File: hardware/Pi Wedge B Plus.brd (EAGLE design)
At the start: 74.9 x 67.3 mm, 14 parts

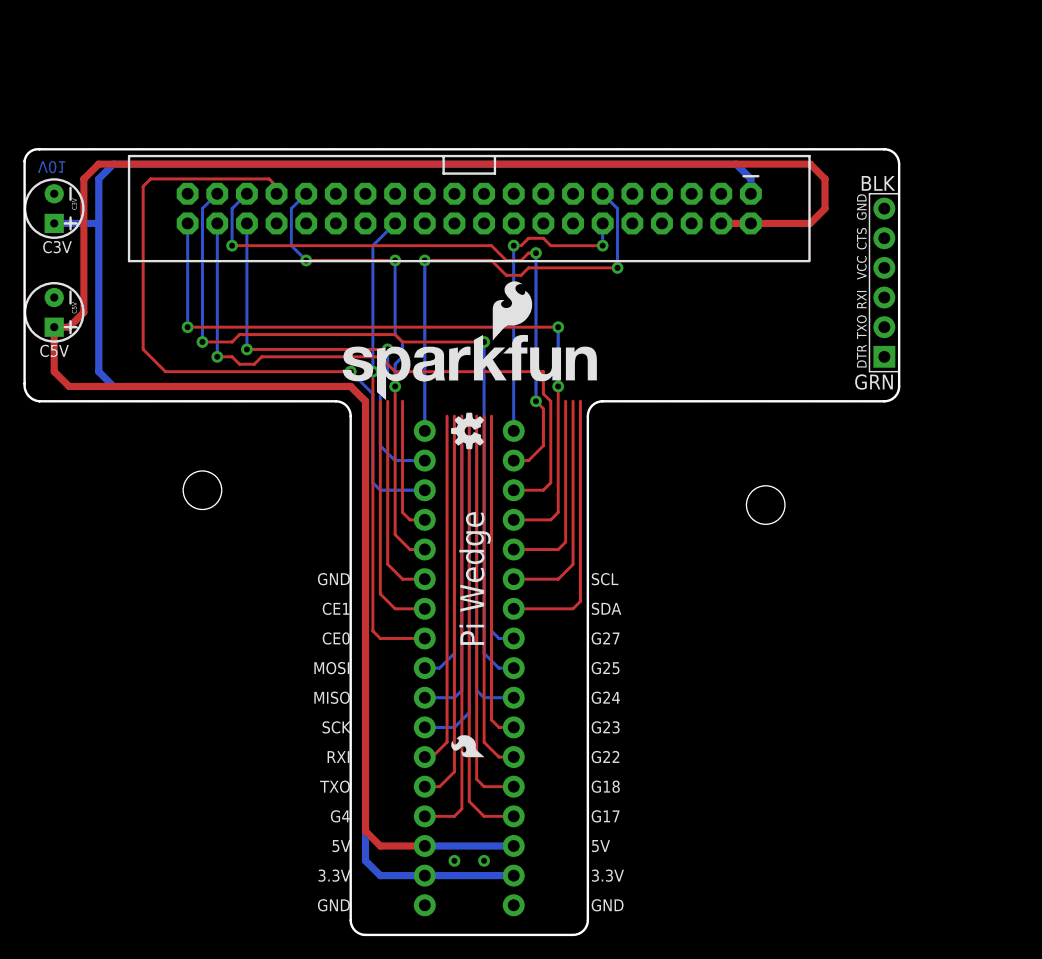
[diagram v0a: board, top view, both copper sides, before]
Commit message: Better routing.
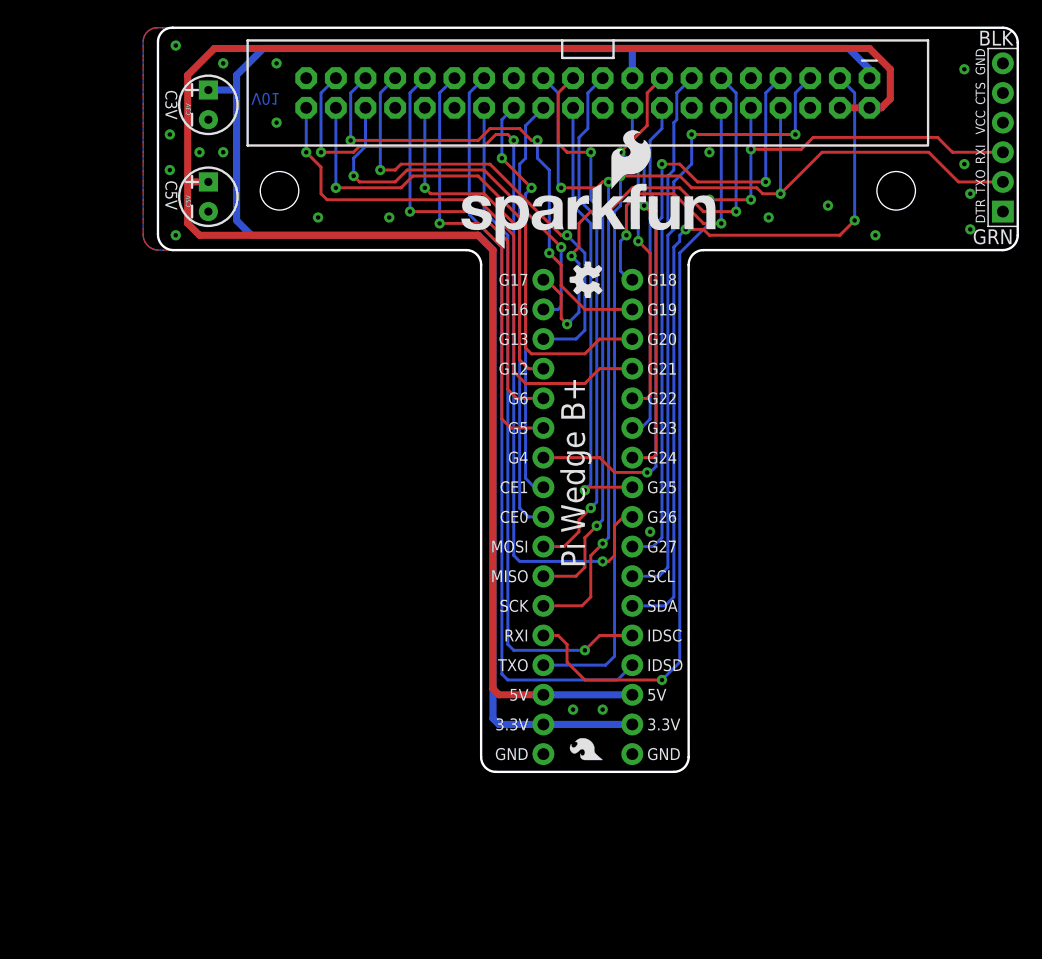
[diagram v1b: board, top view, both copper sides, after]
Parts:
- added LOGO2: SFE_LOGO_NAME_FLAME.2_INCH, SparkFun-Aesthetics:SFE_LOGO_NAME_FLAME_.2
- moved STANDOFF2 29.2 mm to (63.2, 49.8)
- moved STANDOFF1 26.5 mm to (10.4, 49.8)
- moved FRAME2 26.0 mm to (20.3, -8.38)
- moved C5V 16.5 mm to (4.32, 49.3), turned to 90 degrees
- moved U$4 16.5 mm to (33.0, 1.52)
- moved LOGO1 16.5 mm to (25.3, 44.7)
- moved U$1 16.5 mm to (36.8, 42.2)
- moved U$5 16.5 mm to (40.6, 1.52)
- moved U$2 16.5 mm to (36.8, 66.3)
- moved JP4 16.1 mm to (72.4, 54.4)
- moved C3V 15.9 mm to (4.32, 57.1), turned to 90 degrees
- moved U$3 14.2 mm to (36.8, 58.2)
- moved JP1 10.2 mm to (38.1, 1.02)
- moved JP5 10.2 mm to (38.1, 2.92)
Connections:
- net N$2 renamed SCLK
- net N$3 renamed MISO
- net N$4 renamed MOSI
- net N$5 renamed CE0
- net N$6 renamed CE1
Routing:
- net RXI: track 33.5 -> 89.4 mm, vias 0 -> 4
- net TXO: track 37.1 -> 91.1 mm, vias 0 -> 2
- net GP4: track 20.8 -> 55.4 mm, vias 0 -> 3
- net SDA: track 31.0 -> 63.7 mm, vias 0 -> 2
- net SCL: track 28.2 -> 55.5 mm, vias 0 -> 2
- net ID_SD: track 37.4 -> 64.6 mm
- net SCLK: track 30.4 -> 54.9 mm, vias 0 -> 3
- net ID_SC: track 34.6 -> 58.2 mm, vias 0 -> 1
- net MISO: track 27.2 -> 49.7 mm, vias 0 -> 2
- net GP13: track 60.2 -> 39.8 mm, vias 1 -> 2
- net MOSI: track 24.4 -> 44.5 mm, vias 0 -> 1
- net GP5: track 17.7 -> 37.8 mm, vias 0 -> 1
- net GP25: track 18.0 -> 37.8 mm, vias 0 -> 1
- net GP27: track 24.4 -> 43.3 mm
- net GP12: track 11.7 -> 30.0 mm, vias 0 -> 1
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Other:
- board size 74.9 x 67.3 mm -> 73.7 x 63.8 mm
- board text added: "G12"
- board text added: "G13"
- board text added: "G16"
- board text added: "G19"
- board text added: "G20"
- board text added: "G21"
- board text added: "G26"
- board text added: "G5"
- board text added: "G6"
- board text added: "IDSC"
- board text added: "IDSD"
- board text added: "Pi Wedge B+"
- board text removed: "Pi Wedge"

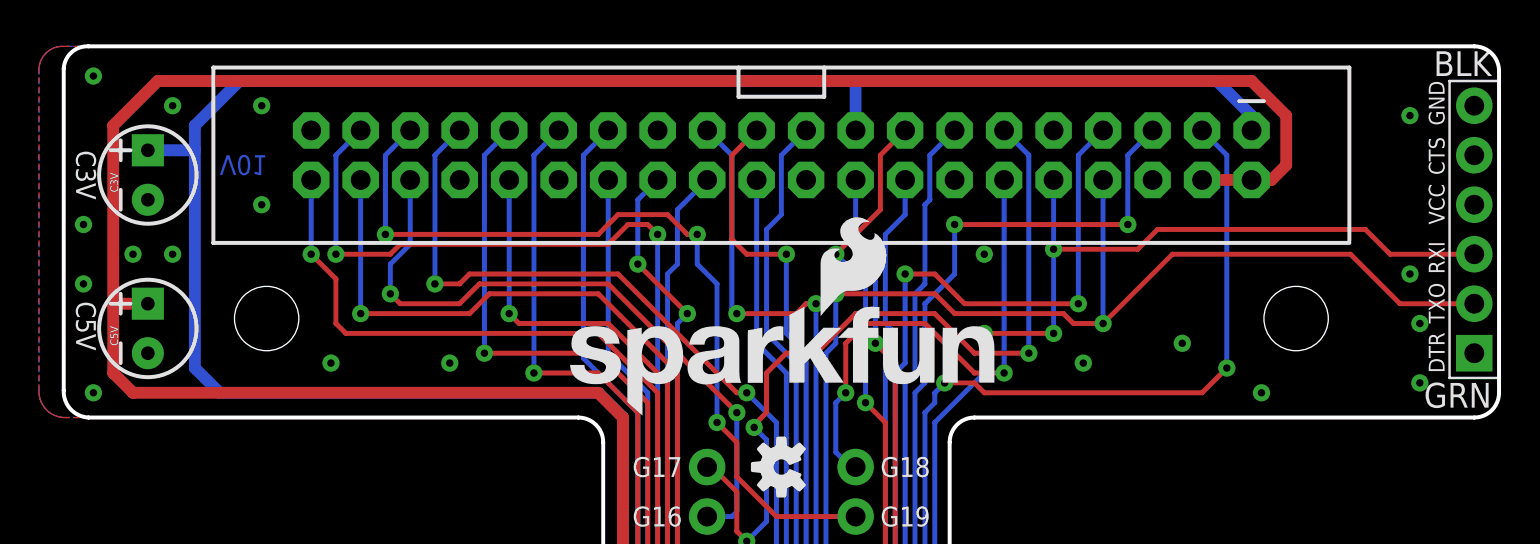
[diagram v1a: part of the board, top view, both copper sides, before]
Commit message: Slight Tweaks to outline
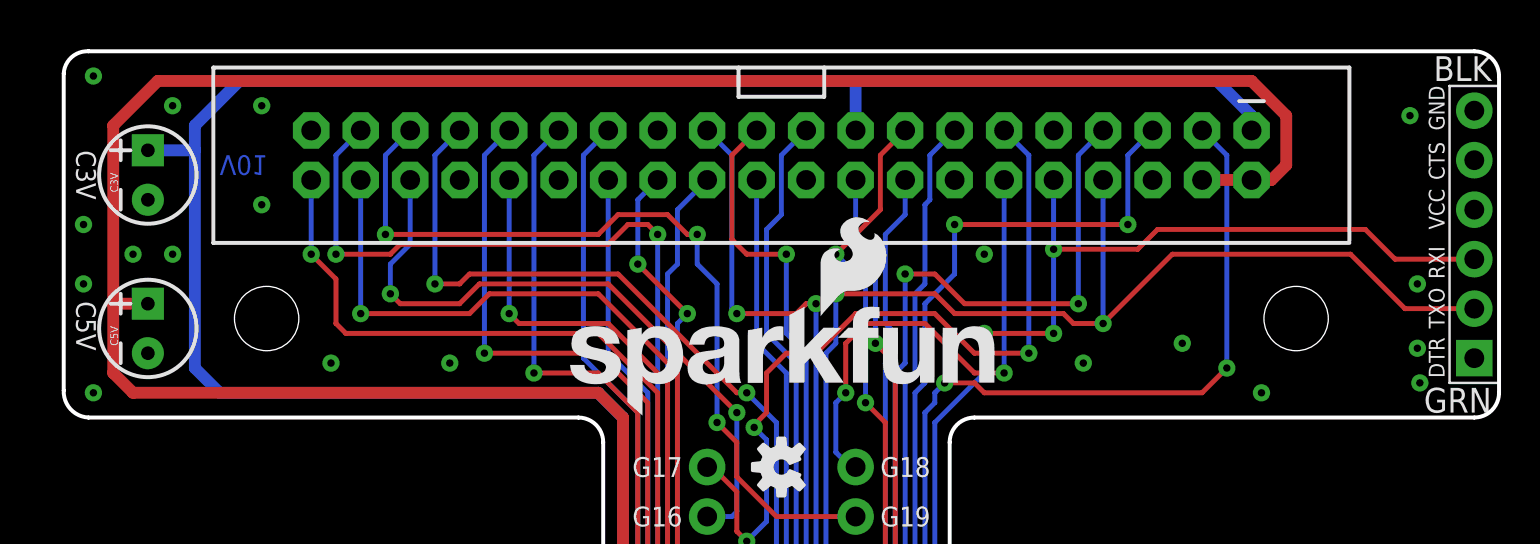
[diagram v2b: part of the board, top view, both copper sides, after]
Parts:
- moved JP4 0.25 mm to (72.4, 54.1)
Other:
- board size 73.7 x 63.8 mm -> 73.7 x 63.5 mm
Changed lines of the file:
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@@
 <setting verticaltext="up"/>
 </settings>
-<grid distance="0.02" unitdist="inch" unit="inch" style="lines" multiple="1" display="yes" altdistance="0.005" altunitdist="inch" altunit="inch"/>
+<grid distance="0.05" unitdist="inch" unit="inch" style="lines" multiple="1" display="yes" altdistance="0.005" altunitdist="inch" altunit="inch"/>
 <layers>
 <layer number="1" name="Top" color="4" fill="1" visible="yes" active="yes"/>
@@
 <layer number="37" name="tTest" color="7" fill="1" visible="no" active="yes"/>
 <layer number="38" name="bTest" color="7" fill="1" visible="no" active="yes"/>
-<layer number="39" name="tKeepout" color="4" fill="11" visible="yes" active="yes"/>
+<layer number="39" name="tKeepout" color="4" fill="11" visible="no" active="yes"/>
 <layer number="40" name="bKeepout" color="1" fill="11" visible="no" active="yes"/>
 <layer number="41" name="tRestrict" color="4" fill="10" visible="no" active="yes"/>
@@
 <board>
 <plain>
-<wire x1="73.66" y1="62.484" x2="73.66" y2="45.974" width="0.2032" layer="20"/>
+<wire x1="73.66" y1="62.23" x2="73.66" y2="45.974" width="0.2032" layer="20"/>
 <wire x1="73.66" y1="45.974" x2="72.39" y2="44.704" width="0.2032" layer="20" curve="-90"/>
 <wire x1="72.39" y1="44.704" x2="46.736" y2="44.704" width="0.2032" layer="20"/>
@@
 <wire x1="44.196" y1="0" x2="45.466" y2="1.27" width="0.2032" layer="20" curve="90"/>
 <wire x1="45.466" y1="1.27" x2="45.466" y2="43.434" width="0.2032" layer="20"/>
-<wire x1="73.66" y1="62.484" x2="72.39" y2="63.754" width="0.2032" layer="20" curve="90"/>
-<wire x1="72.39" y1="63.754" x2="1.27" y2="63.754" width="0.2032" layer="20"/>
-<wire x1="1.27" y1="63.754" x2="0" y2="62.611" width="0.2032" layer="20" curve="90"/>
-<wire x1="0" y1="62.611" x2="0" y2="46.101" width="0.2032" layer="20"/>
+<wire x1="73.66" y1="62.23" x2="72.39" y2="63.5" width="0.2032" layer="20" curve="90"/>
+<wire x1="72.39" y1="63.5" x2="1.27" y2="63.5" width="0.2032" layer="20"/>
+<wire x1="1.27" y1="63.5" x2="0" y2="62.357" width="0.2032" layer="20" curve="90"/>
+<wire x1="0" y1="62.357" x2="0" y2="46.101" width="0.2032" layer="20"/>
 <wire x1="0" y1="46.101" x2="1.27" y2="44.704" width="0.2032" layer="20" curve="90"/>
 <text x="8.001" y="58.166" size="1.016" layer="16" font="vector" ratio="20" rot="SMR180">V01</text>
@@
 <dimension x1="0" y1="69.977" x2="10.414" y2="69.977" x3="5.207" y3="75.692" textsize="1.778" textratio="15" layer="51" unit="inch"/>
 <dimension x1="0" y1="69.977" x2="63.246" y2="69.977" x3="31.623" y3="78.74" textsize="1.778" textratio="15" layer="51" unit="inch"/>
-<dimension x1="73.66" y1="0" x2="73.66" y2="63.754" x3="82.677" y3="31.877" textsize="1.778" textratio="15" layer="51" unit="inch"/>
+<dimension x1="73.66" y1="0" x2="73.66" y2="63.5" x3="82.677" y3="31.75" textsize="1.778" textratio="15" layer="51" unit="inch"/>
 </plain>
 <attributes>
@@
 <element name="U$1" library="SparkFun" package="OSHW-LOGO-S" value="OSHW-LOGOS" x="36.83" y="42.164" rot="R90"/>
 <element name="JP1" library="SparkFun" package="SFE-LOGO-FLAME" value="LOGO-SFESK" x="38.1" y="1.016" rot="R90"/>
-<element name="JP4" library="SparkFun-Connectors" package="FTDI_DEVICE_SIDE" value="FTDI_DEVICE" x="72.39" y="54.356" rot="R90"/>
+<element name="JP4" library="SparkFun-Connectors" package="FTDI_DEVICE_SIDE" value="FTDI_DEVICE" x="72.39" y="54.102" rot="R90"/>
 <element name="FRAME2" library="SparkFun-Aesthetics" package="CREATIVE_COMMONS" value="FRAME-LETTER" x="20.32" y="-8.382"/>
 <element name="LOGO1" library="SparkFun-Aesthetics" package="SFE_LOGO_NAME_FLAME_.2" value="SFE_LOGO_NAME_FLAME.2_INCH" x="25.273" y="44.704"/>
@@
 <contactref element="JP4" pad="P$6"/>
 <polygon width="0.2032" layer="16" isolate="0.3048">
-<vertex x="0" y="44.704"/>
+<vertex x="1.27" y="44.704"/>
 <vertex x="26.416" y="44.704" curve="-90"/>
 <vertex x="27.686" y="43.434"/>
@@
 <vertex x="72.39" y="44.704" curve="90"/>
 <vertex x="73.66" y="45.974"/>
-<vertex x="73.66" y="62.484" curve="90"/>
-<vertex x="72.39" y="63.754"/>
-<vertex x="0" y="63.754" curve="90"/>
-<vertex x="-1.27" y="62.611"/>
-<vertex x="-1.27" y="46.101" curve="90"/>
+<vertex x="73.66" y="62.23" curve="90"/>
+<vertex x="72.39" y="63.5"/>
+<vertex x="1.27" y="63.5" curve="90"/>
+<vertex x="0" y="62.357"/>
+<vertex x="0" y="46.101" curve="90"/>
 </polygon>
 <polygon width="0.2032" layer="1" isolate="0.3048">
@@
 <vertex x="27.686" y="43.434" curve="90"/>
 <vertex x="26.416" y="44.704"/>
-<vertex x="0" y="44.704" curve="-90"/>
-<vertex x="-1.27" y="46.101"/>
-<vertex x="-1.27" y="62.611" curve="-90"/>
-<vertex x="0" y="63.754"/>
-<vertex x="72.39" y="63.754" curve="-90"/>
-<vertex x="73.66" y="62.484"/>
+<vertex x="1.27" y="44.704" curve="-90"/>
+<vertex x="0" y="46.101"/>
+<vertex x="0" y="62.357" curve="-90"/>
+<vertex x="1.27" y="63.5"/>
+<vertex x="72.39" y="63.5" curve="-90"/>
+<vertex x="73.66" y="62.23"/>
 <vertex x="73.66" y="45.974" curve="-90"/>
 <vertex x="72.39" y="44.704"/>
@@
 <via x="38.1" y="5.334" extent="1-16" drill="0.381"/>
 <via x="69.088" y="60.198" extent="1-16" drill="0.381"/>
-<via x="69.596" y="49.53" extent="1-16" drill="0.381"/>
+<via x="69.469" y="48.26" extent="1-16" drill="0.381"/>
 <via x="69.596" y="46.482" extent="1-16" drill="0.381"/>
 <via x="61.468" y="45.974" extent="1-16" drill="0.381"/>
@@
 <via x="42.164" y="20.574" extent="1-16" drill="0.381"/>
 <via x="47.244" y="53.086" extent="1-16" drill="0.381"/>
-<via x="69.088" y="52.07" extent="1-16" drill="0.381"/>
+<via x="69.469" y="51.562" extent="1-16" drill="0.381"/>
 <via x="3.556" y="53.086" extent="1-16" drill="0.381"/>
 <via x="10.16" y="60.706" extent="1-16" drill="0.381"/>
@@
 <wire x1="38.354" y1="9.144" x2="39.116" y2="9.906" width="0.254" layer="16"/>
 <wire x1="39.116" y1="9.906" x2="39.116" y2="48.006" width="0.254" layer="16"/>
-<wire x1="72.39" y1="50.546" x2="68.58" y2="50.546" width="0.254" layer="1"/>
-<wire x1="68.58" y1="50.546" x2="66.04" y2="53.086" width="0.254" layer="1"/>
+<wire x1="72.39" y1="50.292" x2="68.834" y2="50.292" width="0.254" layer="1"/>
+<wire x1="68.834" y1="50.292" x2="66.04" y2="53.086" width="0.254" layer="1"/>
 <wire x1="66.04" y1="53.086" x2="56.896" y2="53.086" width="0.254" layer="1"/>
 <wire x1="56.896" y1="53.086" x2="53.34" y2="49.53" width="0.254" layer="1"/>
@@
 <wire x1="50.8" y1="49.022" x2="50.8" y2="53.34" width="0.254" layer="16"/>
 <wire x1="50.8" y1="53.34" x2="50.8" y2="56.896" width="0.254" layer="16"/>
-<wire x1="72.39" y1="53.086" x2="68.072" y2="53.086" width="0.254" layer="1"/>
-<wire x1="68.072" y1="53.086" x2="66.802" y2="54.356" width="0.254" layer="1"/>
+<wire x1="72.39" y1="52.832" x2="68.326" y2="52.832" width="0.254" layer="1"/>
+<wire x1="68.326" y1="52.832" x2="66.802" y2="54.356" width="0.254" layer="1"/>
 <wire x1="66.802" y1="54.356" x2="56.134" y2="54.356" width="0.254" layer="1"/>
 <wire x1="56.134" y1="54.356" x2="55.118" y2="53.34" width="0.254" layer="1"/>

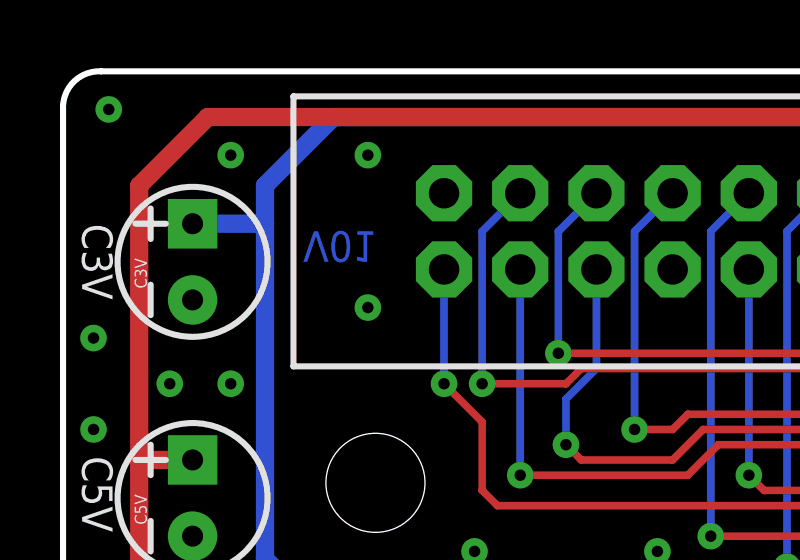
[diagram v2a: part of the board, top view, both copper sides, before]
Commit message: Bumping rev number for reds
From V01 to V10.
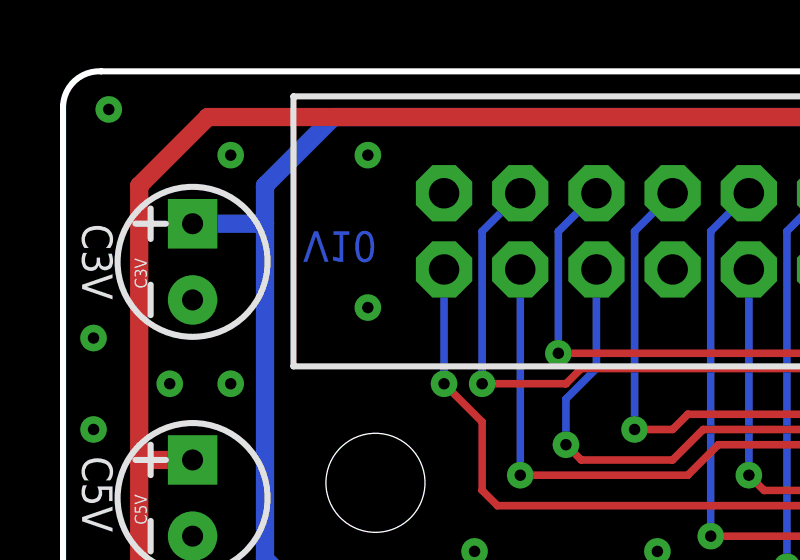
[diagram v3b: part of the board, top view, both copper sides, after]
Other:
- board text added: "V10"
- board text removed: "V01"
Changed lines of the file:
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@@
 <wire x1="0" y1="62.357" x2="0" y2="46.101" width="0.2032" layer="20"/>
 <wire x1="0" y1="46.101" x2="1.27" y2="44.704" width="0.2032" layer="20" curve="90"/>
-<text x="8.001" y="58.166" size="1.016" layer="16" font="vector" ratio="20" rot="SMR180">V01</text>
+<text x="8.001" y="58.166" size="1.016" layer="16" font="vector" ratio="20" rot="SMR180">V10</text>
 <text x="31.75" y="1.524" size="1.016" layer="21" font="vector" ratio="19" rot="SR0" align="center-right">GND</text>
 <text x="36.576" y="25.654" size="2.032" layer="21" font="vector" ratio="19" rot="SR90" align="bottom-center">Pi Wedge B+</text>
